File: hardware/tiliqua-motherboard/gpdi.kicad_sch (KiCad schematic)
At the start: 18 parts, among them J10 DVI_GPDI, U3 PCA9306DP

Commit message: hw/mobo-r3: assign remaining part numbers
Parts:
- R44: lcsc# (none) -> C25764
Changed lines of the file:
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@@
 			)
 		)
-		(property "lcsc#" ""
+		(property "lcsc#" "C25764"
 			(at 114.3 86.36 0)
 			(effects

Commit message: hw/mobo-r3: add LCSC database / associations
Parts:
- D4: LCSC (none) -> C173412
- F3: LCSC (none) -> C883096
- J10: LCSC (none) -> C428493
- R25, R9: LCSC (none) -> C25900
- R26, R31: LCSC (none) -> C474081
- R28: LCSC (none) -> C25744
- R34, R35, R36, R37, R38, R39, R40, R41: LCSC (none) -> C25099
- R44: LCSC (none) -> C25764
- U3: LCSC (none) -> C128835
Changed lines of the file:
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@@
+			)
+		)
+		(property "LCSC" "C25900"
+			(at 117.094 91.694 0)
+			(effects
+				(font
+					(size 1.27 1.27)
+				)
+				(hide yes)
 			)
 		)
@@
 			)
 		)
+		(property "LCSC" "C25099"
+			(at 152.4 72.39 0)
+			(effects
+				(font
+					(size 1.27 1.27)
+				)
+				(hide yes)
+			)
+		)
 		(pin "1"
 		)
@@
 			)
 		)
+		(property "LCSC" "C25099"
+			(at 152.4 80.264 0)
+			(effects
+				(font
+					(size 1.27 1.27)
+				)
+				(hide yes)
+			)
+		)
 		(pin "1"
 		)
@@
 			)
 		)
+		(property "LCSC" "C25099"
+			(at 152.4 85.344 0)
+			(effects
+				(font
+					(size 1.27 1.27)
+				)
+				(hide yes)
+			)
+		)
 		(pin "1"
 		)
@@
 			)
 		)
+		(property "LCSC" "C128835"
+			(at 100.584 110.744 0)
+			(effects
+				(font
+					(size 1.27 1.27)
+				)
+				(hide yes)
+			)
+		)
 		(pin "8"
 		)
@@
 			)
 		)
+		(property "LCSC" "C25099"
+			(at 152.4 82.55 0)
+			(effects
+				(font
+					(size 1.27 1.27)
+				)
+				(hide yes)
+			)
+		)
 		(pin "1"
 		)
@@
 			)
 		)
+		(property "LCSC" "C25099"
+			(at 152.4 74.93 0)
+			(effects
+				(font
+					(size 1.27 1.27)
+				)
+				(hide yes)
+			)
+		)
 		(pin "1"
 		)
@@
 		(property "Tol" ""
 			(at 171.45 60.96 0)
+			(effects
+				(font
+					(size 1.27 1.27)
+				)
+				(hide yes)
+			)
+		)
+		(property "LCSC" "C883096"
+			(at 173.99 60.198 0)
 			(effects
 				(font
@@
 			)
 		)
+		(property "LCSC" "C428493"
+			(at 182.88 90.1699 0)
+			(effects
+				(font
+					(size 1.27 1.27)
+				)
+				(hide yes)
+			)
+		)
 		(pin "14"
 		)
@@
 			)
 		)
+		(property "LCSC" "C25764"
+			(at 112.522 84.074 0)
+			(effects
+				(font
+					(size 1.27 1.27)
+				)
+				(hide yes)
+			)
+		)
 		(pin "1"
 		)
@@
 		(property "Tol" ""
 			(at 157.48 106.68 0)
+			(effects
+				(font
+					(size 1.27 1.27)
+				)
+				(hide yes)
+			)
+		)
+		(property "LCSC" "C25744"
+			(at 159.258 104.394 0)
 			(effects
 				(font
@@
 			)
 		)
+		(property "LCSC" "C25099"
+			(at 152.4 77.47 0)
+			(effects
+				(font
+					(size 1.27 1.27)
+				)
+				(hide yes)
+			)
+		)
 		(pin "1"
 		)
@@
 			)
 		)
+		(property "LCSC" "C474081"
+			(at 159.258 91.694 0)
+			(effects
+				(font
+					(size 1.27 1.27)
+				)
+				(hide yes)
+			)
+		)
 		(pin "1"
 		)
@@
 		(property "Tol" ""
 			(at 124.46 97.79 0)
+			(effects
+				(font
+					(size 1.27 1.27)
+				)
+				(hide yes)
+			)
+		)
+		(property "LCSC" "C25900"
+			(at 127 96.012 0)
 			(effects
 				(font
@@
 			)
 		)
+		(property "LCSC" "C173412"
+			(at 150.114 110.236 0)
+			(effects
+				(font
+					(size 1.27 1.27)
+				)
+				(hide yes)
+			)
+		)
 		(pin "2"
 		)
@@
 			)
 		)
+		(property "LCSC" "C25099"
+			(at 152.4 70.104 0)
+			(effects
+				(font
+					(size 1.27 1.27)
+				)
+				(hide yes)
+			)
+		)
 		(pin "1"
 		)
@@
 		(property "Tol" ""
 			(at 157.48 109.22 0)
+			(effects
+				(font
+					(size 1.27 1.27)
+				)
+				(hide yes)
+			)
+		)
+		(property "LCSC" "C474081"
+			(at 159.004 111.506 0)
 			(effects
 				(font
@@
 			(effects
 				(font
+					(size 1.27 1.27)
+				)
+				(hide yes)
+			)
+		)
+		(property "LCSC" "C25099"
+			(at 152.4 87.63 0)
+			(effects
+				(font

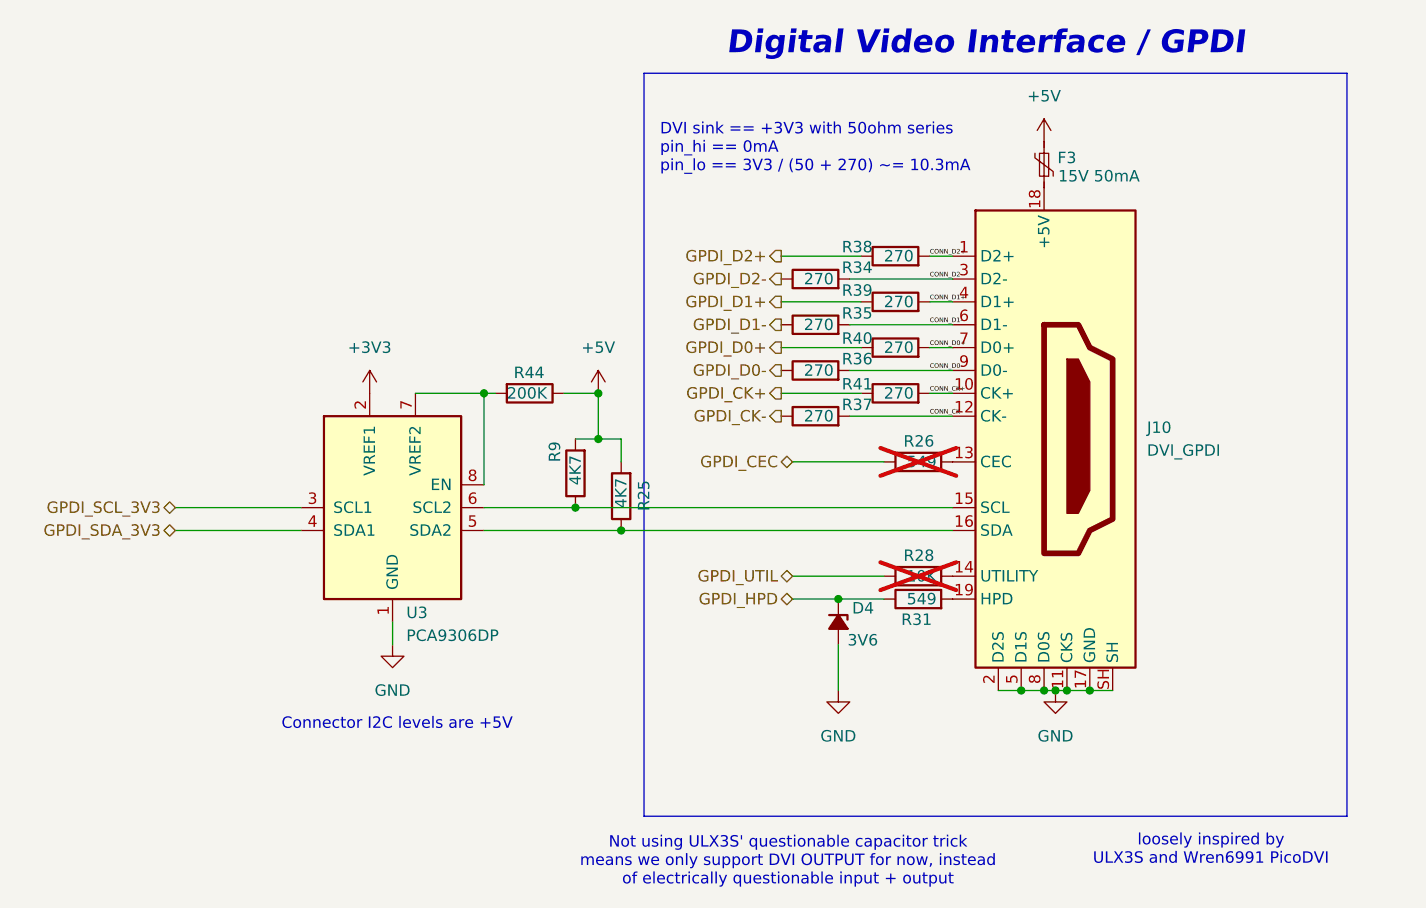
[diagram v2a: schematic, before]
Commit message: * series 27R/33R on all FFC lines * add external PLL SI5351 * pinout changes:     - FFC_SDIN1: 44 -> 42     - ENC_B: 40 -> 12     - ENC_A: 42 -> 8     - PLL_CLK1 -> 40 (removed: spare FPGA to RP2040 line)     - PLL_CLK0 -> 44 (removed: spare FPGA to RP2040 line)
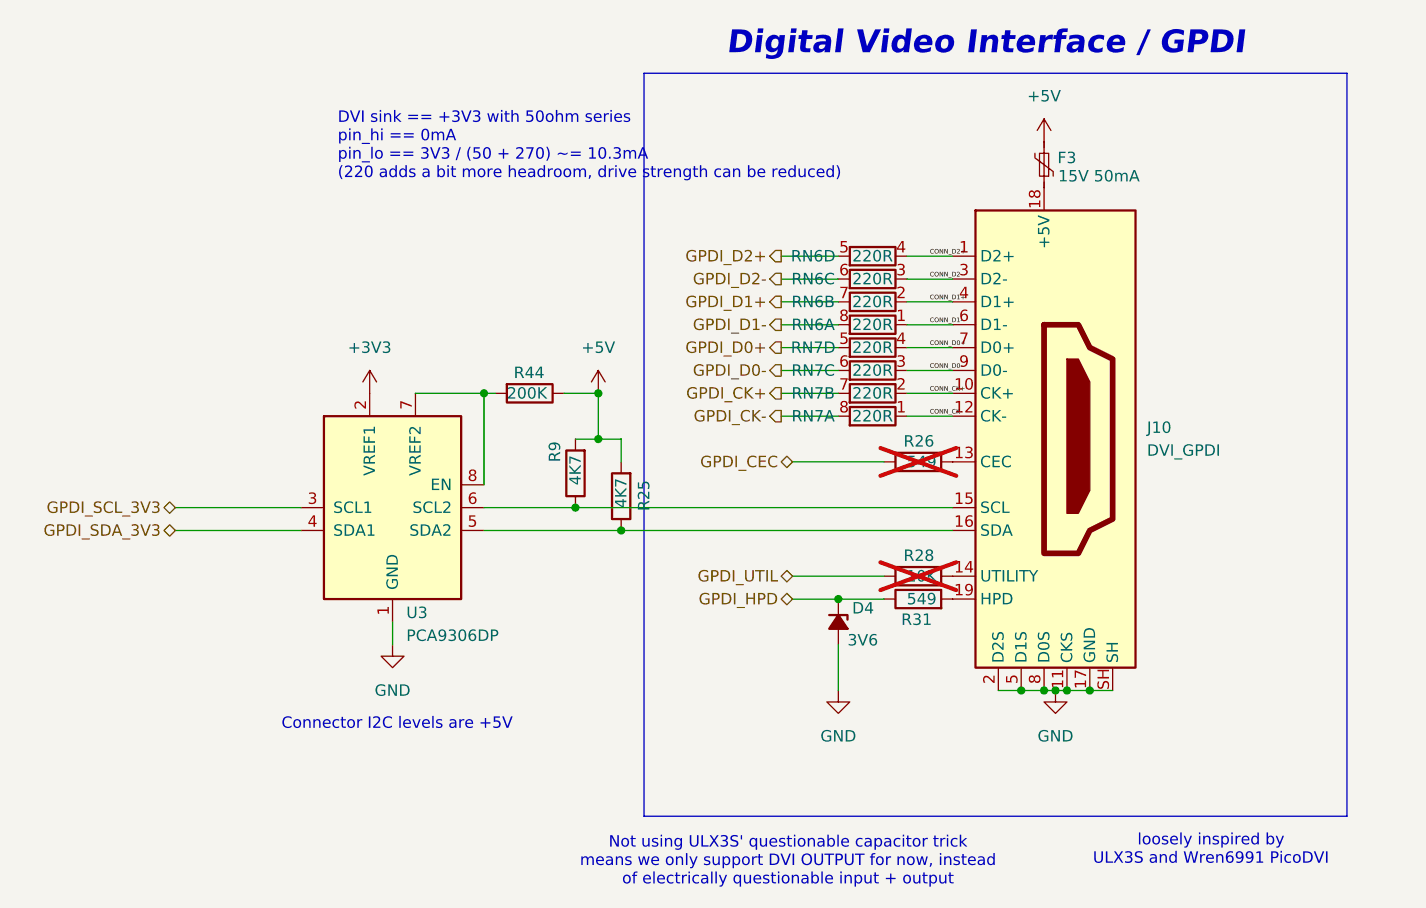
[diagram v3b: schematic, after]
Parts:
- removed R34, R35, R36, R37, R38, R39, R40, R41: 270, Resistor_SMD:R_0402_1005Metric, symbol Device:R
- added RN6, RN7: 220R, Resistor_SMD:R_Array_Convex_4x0402, symbol Device:R_Pack04_Split
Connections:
- net CONN_CK+: now also RN7.2 (R2.1)
- net CONN_CK-: now also RN7.1 (R1.1)
- net CONN_D0+: now also RN7.4 (R4.1)
- net CONN_D0-: now also RN7.3 (R3.1)
- net CONN_D1+: now also RN6.2 (R2.1)
- net CONN_D1-: now also RN6.1 (R1.1)
- net CONN_D2+: now also RN6.4 (R4.1)
- net CONN_D2-: now also RN6.3 (R3.1)
- net GPDI_CK+: now also RN7.7 (R2.2)
- net GPDI_CK-: now also RN7.8 (R1.2)
- net GPDI_D0+: now also RN7.5 (R4.2)
- net GPDI_D0-: now also RN7.6 (R3.2)
- net GPDI_D1+: now also RN6.7 (R2.2)
- net GPDI_D1-: now also RN6.8 (R1.2)
- net GPDI_D2+: now also RN6.5 (R4.2)
- net GPDI_D2-: now also RN6.6 (R3.2)
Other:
- note added: "DVI sink == +3V3 with 50ohm series pin_hi == 0mA pin_lo == 3V3 / (50 + 270) ~= 10.3mA (220 adds a bit more headroom, drive strength can be reduced)"
- note removed: "DVI sink == +3V3 with 50ohm series pin_hi == 0mA pin_lo == 3V3 / (50 + 270) ~= 10.3mA"
